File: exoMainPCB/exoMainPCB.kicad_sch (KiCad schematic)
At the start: 1 part

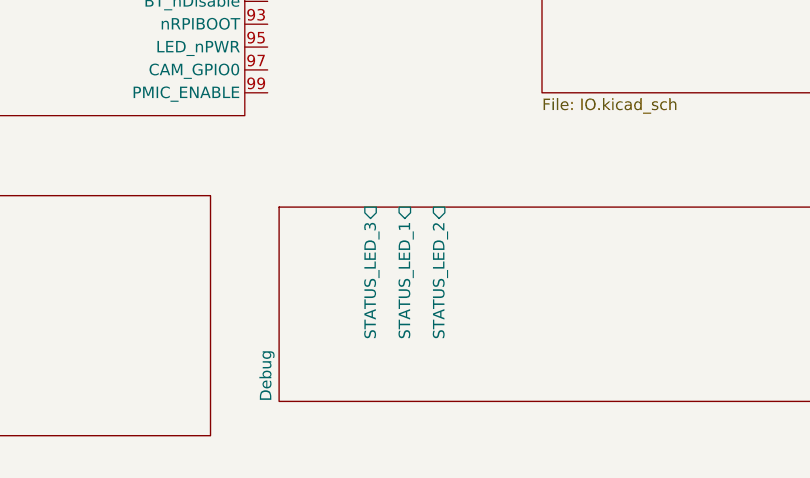
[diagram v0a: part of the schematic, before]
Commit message: finished IMU and added component values
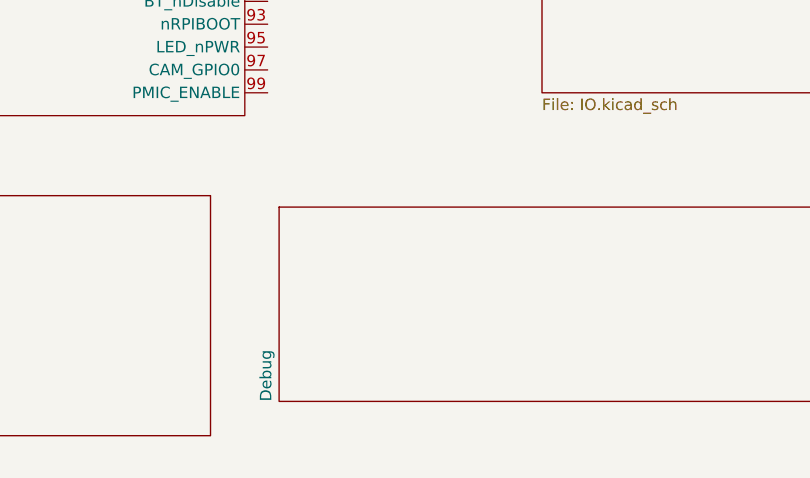
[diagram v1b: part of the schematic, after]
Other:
- sheet Debug ports: added none; removed STATUS_LED_1, STATUS_LED_2, STATUS_LED_3
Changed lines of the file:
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@@
-			)
-		)
-		(pin "STATUS_LED_3" input
-			(at 102.87 166.37 90)
-			(effects
-				(font
-					(size 1.27 1.27)
-				)
-				(justify right)
-			)
-		)
-		(pin "STATUS_LED_1" input
-			(at 106.68 166.37 90)
-			(effects
-				(font
-					(size 1.27 1.27)
-				)
-				(justify right)
-			)
-		)
-		(pin "STATUS_LED_2" input
-			(at 110.49 166.37 90)
-			(effects
-				(font
-					(size 1.27 1.27)
-				)
-				(justify right)
 			)
 		)
